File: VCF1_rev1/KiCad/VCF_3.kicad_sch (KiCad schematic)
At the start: 20 parts, among them U10 CEM3350, U13 74HC4053, U14 Opamp_Quad

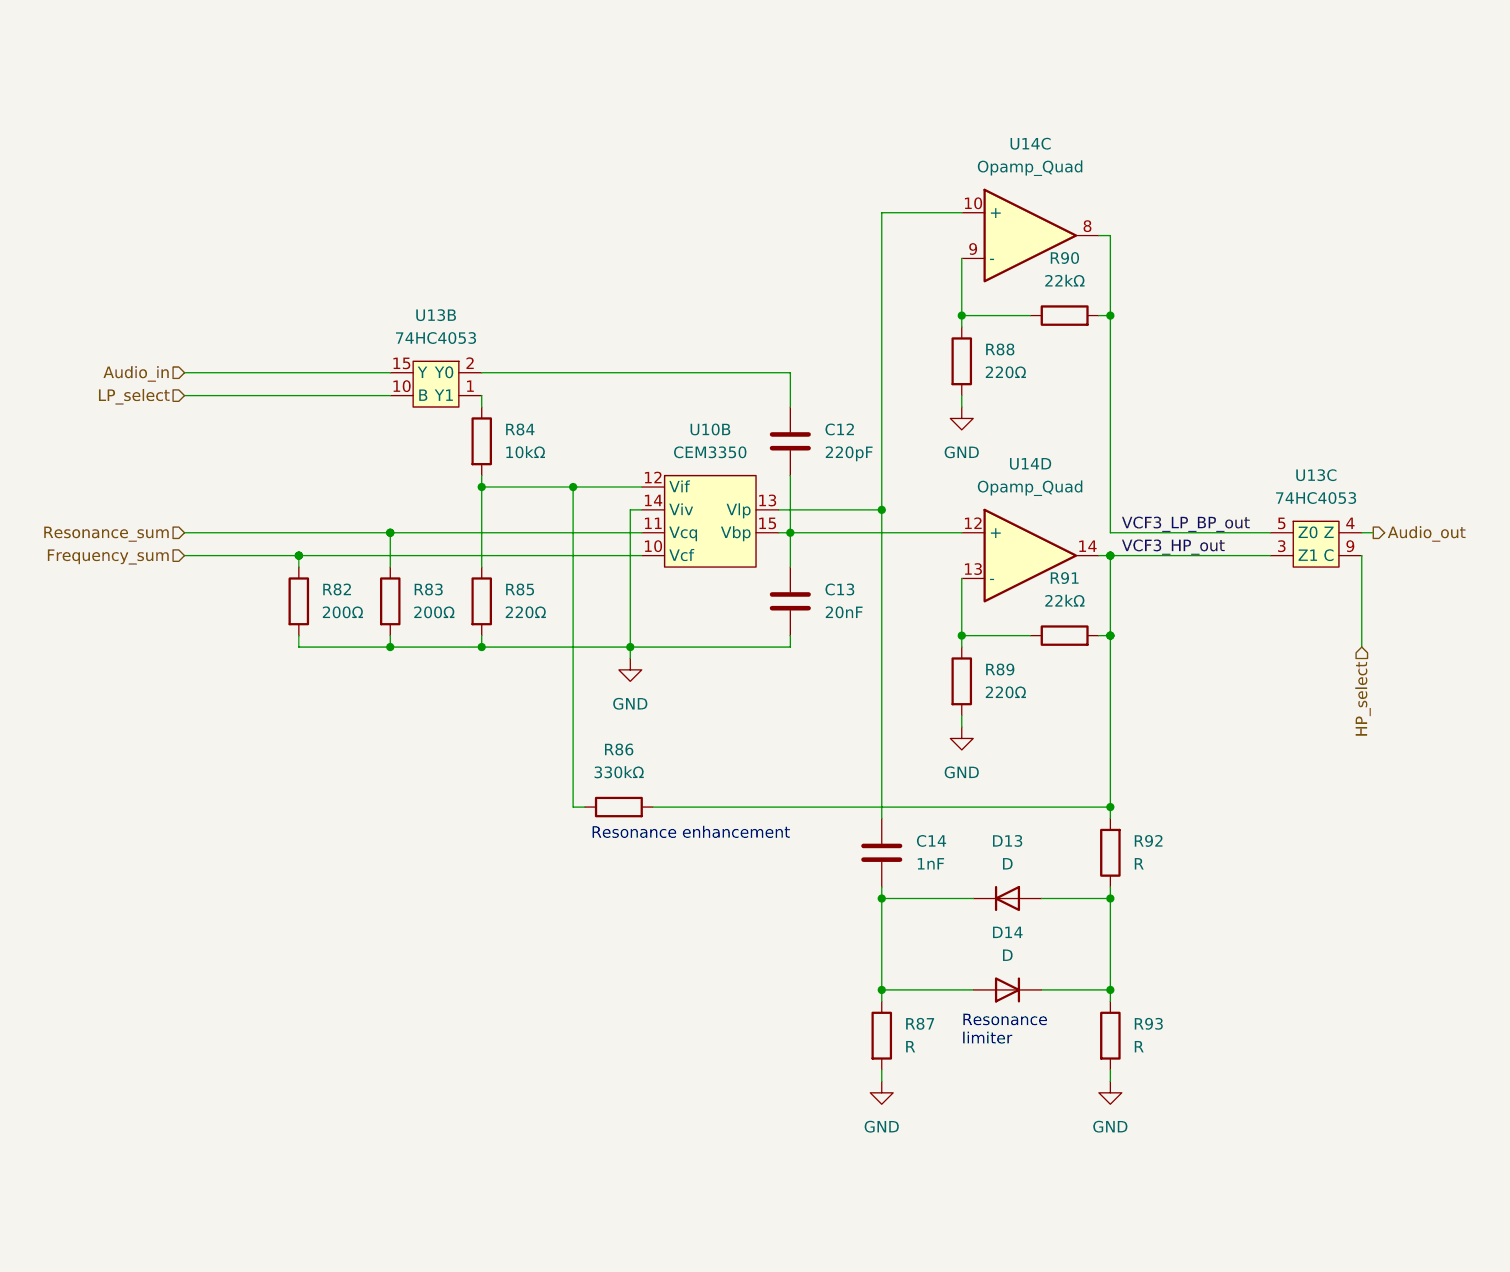
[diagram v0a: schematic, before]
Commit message: Started to populate the PCB and done some small fixes in the schematics.
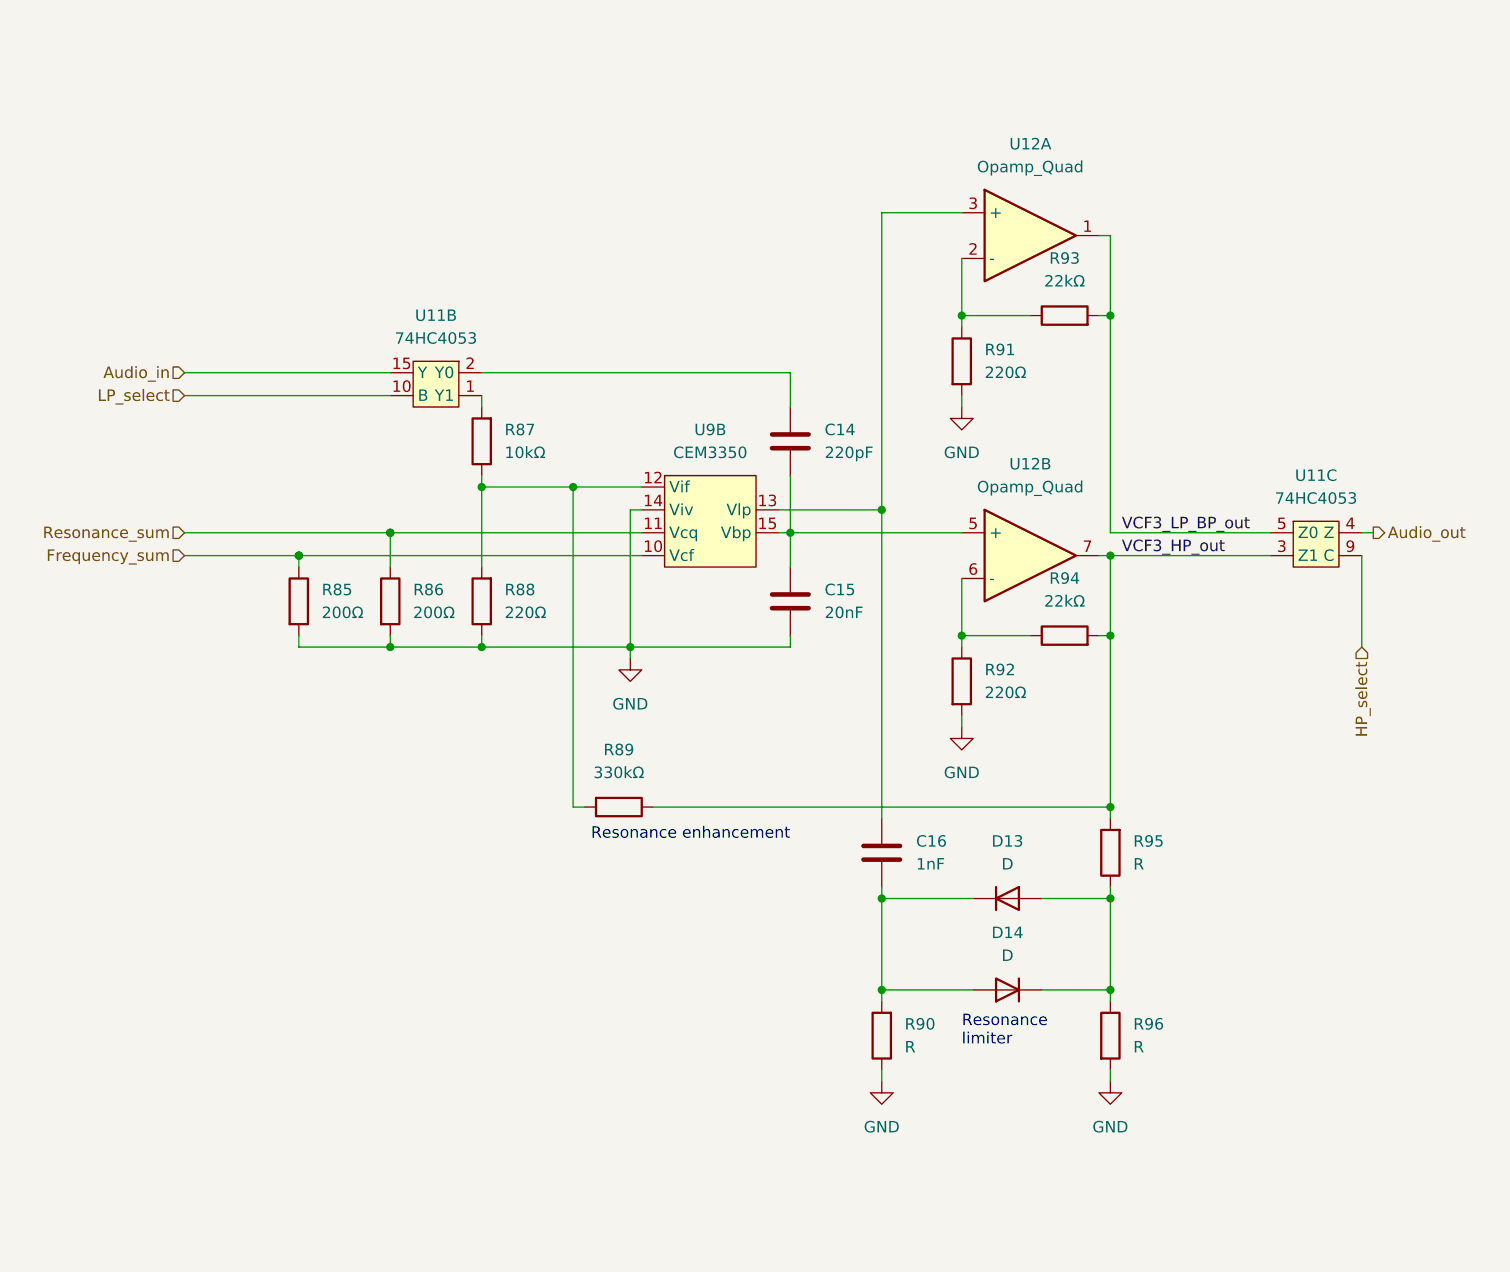
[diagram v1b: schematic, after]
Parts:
- removed R86: 330kΩ, Resistor_SMD:R_0603_1608Metric, symbol Device:R
- added R89: 330kΩ, Resistor_SMD:R_0603_1608Metric, symbol Device:R
- C14: renamed from C12; footprint (none) -> Capacitor_SMD:C_0603_1608Metric
- C15: renamed from C13; footprint (none) -> Capacitor_SMD:C_0603_1608Metric
- C16: renamed from C14; footprint (none) -> Capacitor_SMD:C_0603_1608Metric
- D13, D14: footprint (none) -> Diode_SMD:D_SOD-123
- U11: renamed from U13; footprint (none) -> Package_SO:SOIC-16_3.9x9.9mm_P1.27mm
- U12: renamed from U14; footprint (none) -> Package_SO:SOIC-14_3.9x8.7mm_P1.27mm
- U9: renamed from U10; footprint (none) -> Package_SO:SOIC-16_3.9x9.9mm_P1.27mm
- renumbered R82 to R85, R83 to R86, R84 to R87, R85 to R88, R87 to R90, R88 to R91, R89 to R92, R90 to R93, R91 to R94, R92 to R95, R93 to R96
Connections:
- net GND: now also C15.1, R88.1, R90.1; no longer C15.2, R88.2, R90.2
- net VCF3_HP_out: now also R94.2, R95.2, U12.7, R89.1
- net VCF3_LP_BP_out: now also U12.1; no longer U12.8
- net at D13.1 (K), D14.2 (A): now also C16.2, R90.2; no longer C16.1, R90.1
- net at R92.1, R94.1: now also U12.6 (-); no longer U12.13 (-)
- net at R91.1, R93.1: now also U12.2 (-); no longer U12.9 (-)
- net at C14.1: now also C15.2, U12.5 (+), U9.15 (Vbp); no longer U11.2 (Y0)
- net at U11.1 (Y1): now also R87.2; no longer R87.1
- new net: C16.1, U12.3 (+), U9.13 (Vlp)
- new net: C14.2, U11.2 (Y0)
- new net: R87.1, R88.2, R89.2, U9.12 (Vif)
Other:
- moved on the sheet: C14, C15, C16, R87, R88, R90

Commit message: Placed more components on the PCB.
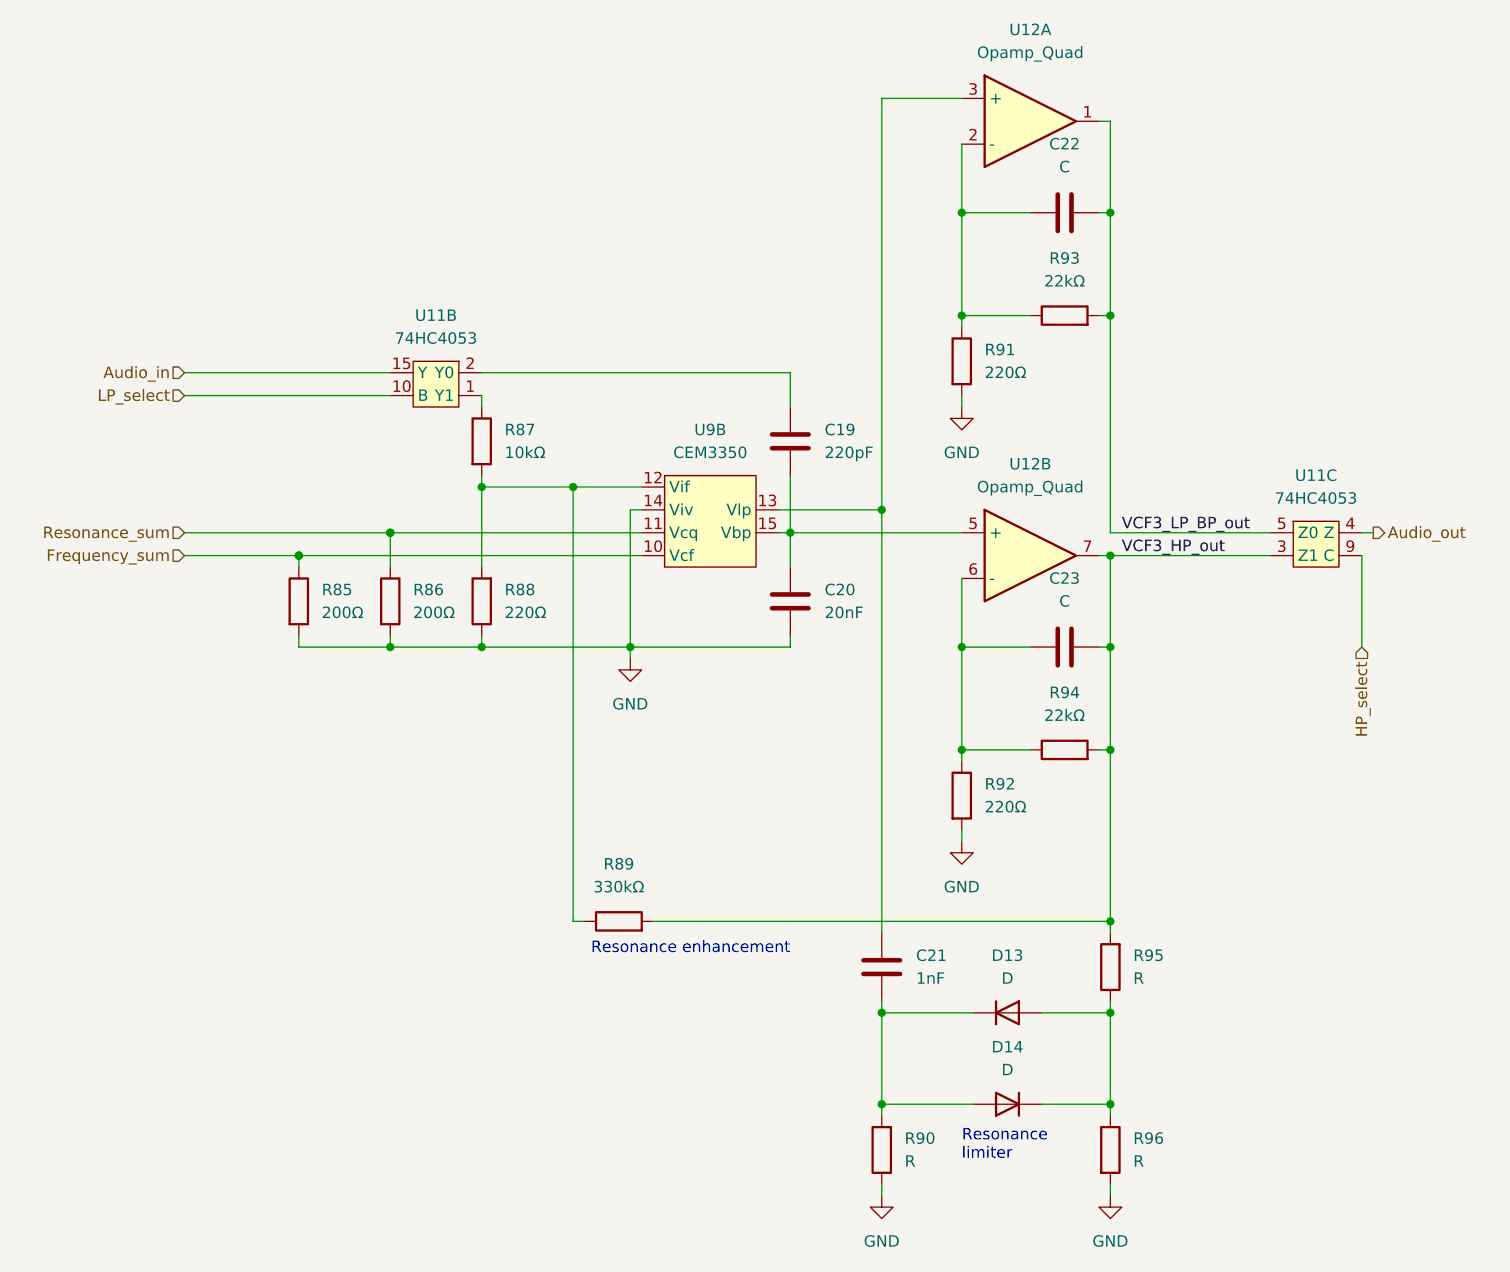
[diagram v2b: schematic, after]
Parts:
- added C22, C23: C, Capacitor_SMD:C_0603_1608Metric, symbol Device:C
- renumbered C14 to C19, C15 to C20, C16 to C21
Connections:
- net VCF3_HP_out: now also R89.2, C23.2; no longer R89.1
- net VCF3_LP_BP_out: now also C22.2
- net at U12.3 (+), U9.13 (Vlp): now also C21.2; no longer C21.1
- net at D13.1 (K), D14.2 (A), R90.2: now also C21.1; no longer C21.2
- net at R92.1, R94.1, U12.6 (-): now also C23.1
- net at R91.1, R93.1, U12.2 (-): now also C22.1
- net at C20.2, U12.5 (+), U9.15 (Vbp): now also C19.2; no longer C19.1
- net at U11.2 (Y0): now also C19.1; no longer C19.2
- net at U11.1 (Y1): now also R87.1; no longer R87.2
- net at R88.2, U9.12 (Vif): now also R87.2, R89.1; no longer R87.1, R89.2
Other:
- moved on the sheet: C19, C21, D13, D14, R87, R89, R90, R92, R94, R95, R96, U12A
